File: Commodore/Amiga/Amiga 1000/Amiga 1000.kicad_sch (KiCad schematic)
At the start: 434 parts, among them J1 COMP, J10 DISK 0, J11 RIGHT (1), J12 LEFT (0), J13 D0 PWR, J14 DC POWER, J15 CONN_LED, J2 RF MOD, J3 RGB, J4 L, J5 R, J6 SERIAL, J7 DISK 1, J8 PARALLEL, J9 KBD, P1 CONN_EXPANSION, P1 RAM EXPANSION, Q1 2SC2926, Q10 2SC945A, Q18 2SA733, Q2 2SC2926, Q3 2SC2926, Q4 2SC945A, Q5 2SC945A, Q8 2SC752G, Q9 2SB825, T1 166NNF-10264AG, U1H 74F138, U1I 74F138, U1J 74F399, U1M 74LS157, U2H 74F374, U2I 74F257_U2I_J, U2J 74F257_U2I_J, U3G 74LS244_U3G, U3H 74LS373_U3H, U3I 74LS244_U3I, U3J 74LS373_U3J, U4A MOS8362, U4C MOS8361, U4E MOS8364, U4H- 74F74, U4J 74LS244, U4M- LM2901, U5A 74HC244, U5G- LF347, U5L PALEN - U5L, U5M PALCAS - U5M, U5N 23256, U5P 23256, U6A 74HC244, U6K LM1488, U6K- LM1488, U6L- LM1489A, U6M- 74LS32, U6N MOS8520, U6P MOS8520, U6S Motorola_68000, U7A MC1377, U7F- 74LS04, U7M- 74LS04, U7N- 7407, U7P- 7438, U7R- 7407, U8G- 74F74, U8H- 74F74, U8I- 74F74, U9G- 74S51, U9I- 74S51

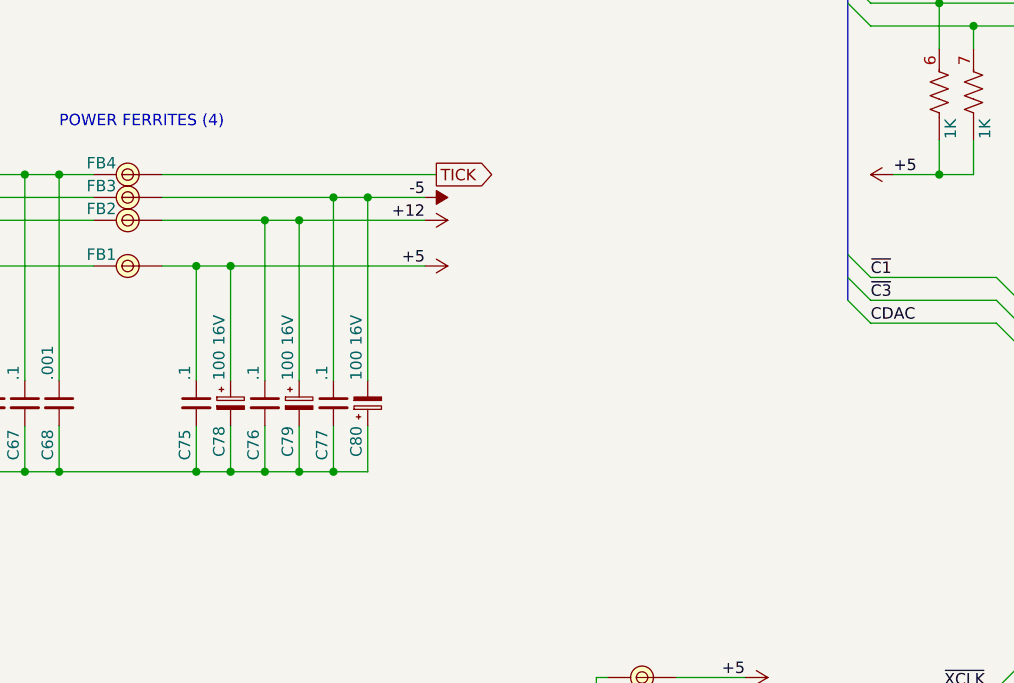
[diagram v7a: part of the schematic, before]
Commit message: Forgot the 26 caps on the power input - Amiga 1000
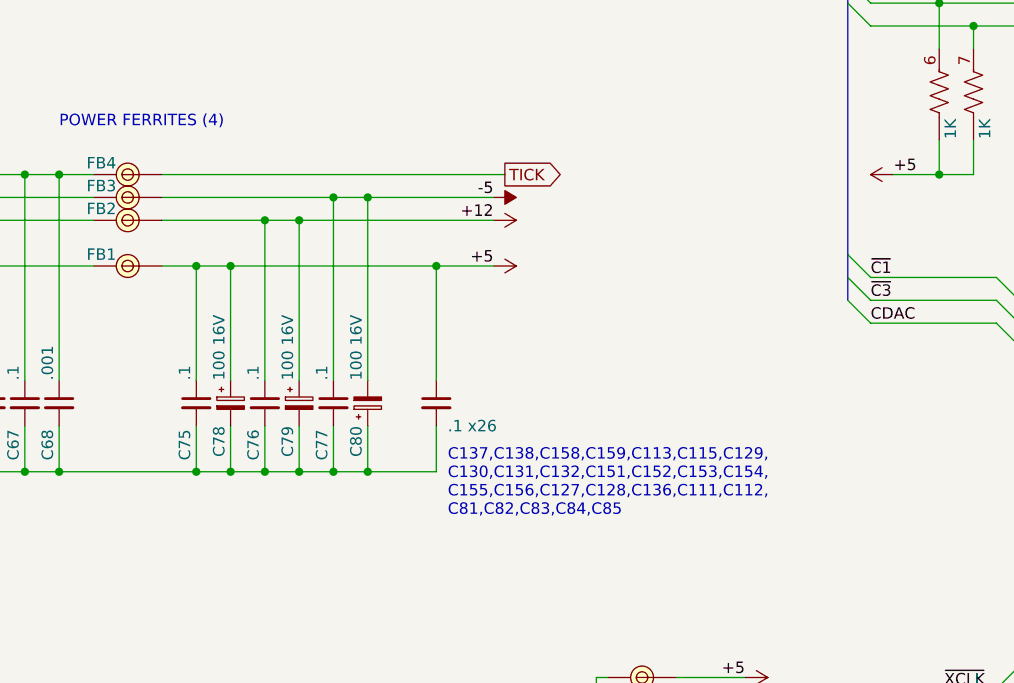
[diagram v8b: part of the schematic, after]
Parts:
- added C137,C138,C158,C159,C113,C115,C129,C130,C131,C132,C151,C152,C153,C154,C155,C156,C127,C128,C136,C111,C112,C81,C82,C83,C84,C85: .1 x26, symbol Device:C_Small
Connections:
- net +5V: now also C137,C138,C158,C159,C113,C115,C129,C130,C131,C132,C151,C152,C153,C154,C155,C156,C127,C128,C136,C111,C112,C81,C82,C83,C84,C85.1
- net GND: now also C137,C138,C158,C159,C113,C115,C129,C130,C131,C132,C151,C152,C153,C154,C155,C156,C127,C128,C136,C111,C112,C81,C82,C83,C84,C85.2
- net at U5N.20 (~{CE}), U5P.20 (~{CE}), W5.: now also U7F-.13, W4.
- net at ROM2.4 (~{WE}): no longer ROM1.4 (~{WE})
- net at ROM2.5 (~{RAS}): no longer ROM1.5 (~{RAS})
- new net: U5N.26 (A14), U5P.26 (A14), W3.
- new net: U5N.20 (~{CE}), U5P.20 (~{CE}), W5.
- new net: U5N.27 (A15), U5P.27 (A15), W1., W2.
- new net: ROM1.4 (~{WE}), ROM2.4 (~{WE})
- new net: ROM1.5 (~{RAS}), ROM2.5 (~{RAS})
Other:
- note added: "C137,C138,C158,C159,C113,C115,C129, C130,C131,C132,C151,C152,C153,C154, C155,C156,C127,C128,C136,C111,C112, C81,C82,C83,C84,C85"
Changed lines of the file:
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@@
   (junction (at 901.7 220.98) (diameter 0) (color 0 0 0 0)
   )
+  (junction (at 121.92 487.68) (diameter 0) (color 0 0 0 0)
+  )
   (junction (at 808.99 64.77) (diameter 0) (color 0 0 0 0)
   )
@@
   (junction (at 466.09 111.76) (diameter 0) (color 0 0 0 0)
   )
+  (junction (at 129.54 464.82) (diameter 0) (color 0 0 0 0)
+  )
   (junction (at 1395.73 335.28) (diameter 0) (color 0 0 0 0)
   )
@@
     (stroke (width 0) (type default) (color 0 0 0 0))
   )
+  (wire (pts (xy 129.54 482.6) (xy 129.54 487.68))
+    (stroke (width 0) (type default) (color 0 0 0 0))
+  )
   (wire (pts (xy 69.85 264.16) (xy 78.74 264.16))
     (stroke (width 0) (type default) (color 0 0 0 0))
@@
     (stroke (width 0) (type default) (color 0 0 0 0))
   )
-  (wire (pts (xy 99.06 454.66) (xy 129.54 454.66))
+  (wire (pts (xy 99.06 454.66) (xy 137.16 454.66))
     (stroke (width 0) (type default) (color 0 0 0 0))
   )
@@
     (stroke (width 0) (type default) (color 0 0 0 0))
   )
+  (wire (pts (xy 129.54 487.68) (xy 121.92 487.68))
+    (stroke (width 0) (type default) (color 0 0 0 0))
+  )
   (wire (pts (xy 817.88 224.79) (xy 836.93 224.79))
     (stroke (width 0) (type default) (color 0 0 0 0))
@@
     (stroke (width 0) (type default) (color 0 0 0 0))
   )
-  (wire (pts (xy 121.92 457.2) (xy 128.27 457.2))
+  (wire (pts (xy 121.92 457.2) (xy 135.89 457.2))
     (stroke (width 0) (type default) (color 0 0 0 0))
   )
@@
     (stroke (width 0) (type default) (color 0 0 0 0))
   )
-  (wire (pts (xy 106.68 464.82) (xy 128.27 464.82))
+  (wire (pts (xy 106.68 464.82) (xy 129.54 464.82))
     (stroke (width 0) (type default) (color 0 0 0 0))
   )
@@
     (stroke (width 0) (type default) (color 0 0 0 0))
   )
+  (wire (pts (xy 129.54 464.82) (xy 135.89 464.82))
+    (stroke (width 0) (type default) (color 0 0 0 0))
+  )
   (wire (pts (xy 440.69 82.55) (xy 435.61 82.55))
     (stroke (width 0) (type default) (color 0 0 0 0))
@@
     (stroke (width 0) (type default) (color 0 0 0 0))
   )
+  (wire (pts (xy 129.54 477.52) (xy 129.54 464.82))
+    (stroke (width 0) (type default) (color 0 0 0 0))
+  )
   (wire (pts (xy 1010.92 233.68) (xy 1007.11 233.68))
     (stroke (width 0) (type default) (color 0 0 0 0))
@@
     (stroke (width 0) (type default) (color 0 0 0 0))
   )
-  (wire (pts (xy 114.3 459.74) (xy 128.27 459.74))
+  (wire (pts (xy 114.3 459.74) (xy 135.89 459.74))
     (stroke (width 0) (type default) (color 0 0 0 0))
   )
@@
     (effects (font (size 1.27 1.27)) (justify left bottom))
   )
+  (text "C137,C138,C158,C159,C113,C115,C129,\nC130,C131,C132,C151,C152,C153,C154,\nC155,C156,C127,C128,C136,C111,C112,\nC81,C82,C83,C84,C85"
+    (at 130.81 492.76 0)
+    (effects (font (size 1.27 1.27)) (justify left bottom))
+  )
   (text "470pF\nx13" (at 584.2 92.71 0)
     (effects (font (size 1.27 1.27)) (justify left bottom))
@@
     (effects (font (size 1.27 1.27)) (justify left bottom))
   )
-  (label "+5" (at 128.27 464.82 180)
+  (label "+5" (at 135.89 464.82 180)
     (effects (font (size 1.27 1.27)) (justify right bottom))
   )
@@
     (effects (font (size 1.27 1.27)) (justify right bottom))
   )
-  (label "+12" (at 128.27 459.74 180)
+  (label "+12" (at 135.89 459.74 180)
     (effects (font (size 1.27 1.27)) (justify right bottom))
   )
@@
     (effects (font (size 1.27 1.27)) (justify left bottom))
   )
-  (label "-5" (at 128.27 457.2 180)
+  (label "-5" (at 135.89 457.2 180)
     (effects (font (size 1.27 1.27)) (justify right bottom))
   )
@@
     )
   )
-  (global_label "TICK" (shape output) (at 129.54 454.66 0) (fields_autoplaced)
+  (global_label "TICK" (shape output) (at 137.16 454.66 0) (fields_autoplaced)
     (effects (font (size 1.27 1.27)) (justify left))
-    (property "Intersheet References" "${INTERSHEET_REFS}" (id 0) (at 136.0655 454.5806 0)
+    (property "Intersheet References" "${INTERSHEET_REFS}" (id 0) (at 143.6855 454.5806 0)
       (effects (font (size 1.27 1.27)) (justify left) hide)
     )
@@
     (pin "2")
   )
+  (symbol (lib_id "Device:C_Small") (at 129.54 480.06 0) (unit 1)
+    (in_bom yes) (on_board yes)
+    (property "Reference" "C137,C138,C158,C159,C113,C115,C129,C130,C131,C132,C151,C152,C153,C154,C155,C156,C127,C128,C136,C111,C112,C81,C82,C83,C84,C85" (id 0) (at 130.81 476.25 0)
+      (effects (font (size 1.27 1.27)) (justify left) hide)
+    )
+    (property "Value" ".1 x26" (id 1) (at 130.81 482.6 0)
+      (effects (font (size 1.27 1.27)) (justify left))
+    )
+    (property "Footprint" "" (id 2) (at 129.54 480.06 0)
+      (effects (font (size 1.27 1.27)) hide)
+    )
+    (property "Datasheet" "~" (id 3) (at 129.54 480.06 0)
+      (effects (font (size 1.27 1.27)) hide)
+    )
+    (pin "1")
+    (pin "2")
+  )
   (symbol (lib_id "power:+5V") (at 920.75 407.67 270) (unit 1)
     (in_bom yes) (on_board yes) (fields_autoplaced)
@@
     (pin "1")
   )
-  (symbol (lib_id "power:+12V") (at 128.27 459.74 270) (unit 1)
+  (symbol (lib_id "power:+12V") (at 135.89 459.74 270) (unit 1)
     (in_bom yes) (on_board yes) (fields_autoplaced)
-    (property "Reference" "#PWR0187" (id 0) (at 124.46 459.74 0)
+    (property "Reference" "#PWR0187" (id 0) (at 132.08 459.74 0)
       (effects (font (size 1.27 1.27)) hide)
     )
-    (property "Value" "+12V" (id 1) (at 132.08 459.7399 90)
+    (property "Value" "+12V" (id 1) (at 139.7 459.7399 90)
       (effects (font (size 1.27 1.27)) (justify left) hide)
     )
-    (property "Footprint" "" (id 2) (at 128.27 459.74 0)
+    (property "Footprint" "" (id 2) (at 135.89 459.74 0)
       (effects (font (size 1.27 1.27)) hide)
     )
-    (property "Datasheet" "" (id 3) (at 128.27 459.74 0)
+    (property "Datasheet" "" (id 3) (at 135.89 459.74 0)
       (effects (font (size 1.27 1.27)) hide)
     )
@@
     (pin "2")
   )
-  (symbol (lib_id "power:-5V") (at 128.27 457.2 270) (unit 1)
+  (symbol (lib_id "power:-5V") (at 135.89 457.2 270) (unit 1)
     (in_bom yes) (on_board yes) (fields_autoplaced)
-    (property "Reference" "#PWR0186" (id 0) (at 130.81 457.2 0)
+    (property "Reference" "#PWR0186" (id 0) (at 138.43 457.2 0)
       (effects (font (size 1.27 1.27)) hide)
     )
-    (property "Value" "-5V" (id 1) (at 132.08 457.1999 90)
+    (property "Value" "-5V" (id 1) (at 139.7 457.1999 90)
       (effects (font (size 1.27 1.27)) (justify left) hide)
     )
-    (property "Footprint" "" (id 2) (at 128.27 457.2 0)
+    (property "Footprint" "" (id 2) (at 135.89 457.2 0)
       (effects (font (size 1.27 1.27)) hide)
     )
-    (property "Datasheet" "" (id 3) (at 128.27 457.2 0)
+    (property "Datasheet" "" (id 3) (at 135.89 457.2 0)
       (effects (font (size 1.27 1.27)) hide)
     )
@@
     (pin "")
   )
-  (symbol (lib_id "power:+5V") (at 128.27 464.82 270) (unit 1)
+  (symbol (lib_id "power:+5V") (at 135.89 464.82 270) (unit 1)
     (in_bom yes) (on_board yes) (fields_autoplaced)
-    (property "Reference" "#PWR0188" (id 0) (at 124.46 464.82 0)
+    (property "Reference" "#PWR0188" (id 0) (at 132.08 464.82 0)
       (effects (font (size 1.27 1.27)) hide)
     )
-    (property "Value" "+5V" (id 1) (at 132.08 464.8199 90)
+    (property "Value" "+5V" (id 1) (at 139.7 464.8199 90)
       (effects (font (size 1.27 1.27)) (justify left) hide)
     )
-    (property "Footprint" "" (id 2) (at 128.27 464.82 0)
+    (property "Footprint" "" (id 2) (at 135.89 464.82 0)
       (effects (font (size 1.27 1.27)) hide)
     )
-    (property "Datasheet" "" (id 3) (at 128.27 464.82 0)
+    (property "Datasheet" "" (id 3) (at 135.89 464.82 0)
       (effects (font (size 1.27 1.27)) hide)
     )
@@
       (reference "C135") (unit 1) (value "10 10V") (footprint "")
     )
+    (path "/1e385a2e-4b4b-4bbb-8c4a-3797bf10b43a"
+      (reference "C137,C138,C158,C159,C113,C115,C129,C130,C131,C132,C151,C152,C153,C154,C155,C156,C127,C128,C136,C111,C112,C81,C82,C83,C84,C85") (unit 1) (value ".1 x26") (footprint "")
+    )
     (path "/1e88efab-1604-4705-babe-7c91675a6ad2"
